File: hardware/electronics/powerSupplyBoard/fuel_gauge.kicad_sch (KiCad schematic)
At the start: 20 parts, among them J11 PREC002SAAN-RC, Q4 BSS84, Q5 2N7002, Q6 2N7002, U6 BQ34Z100-R2

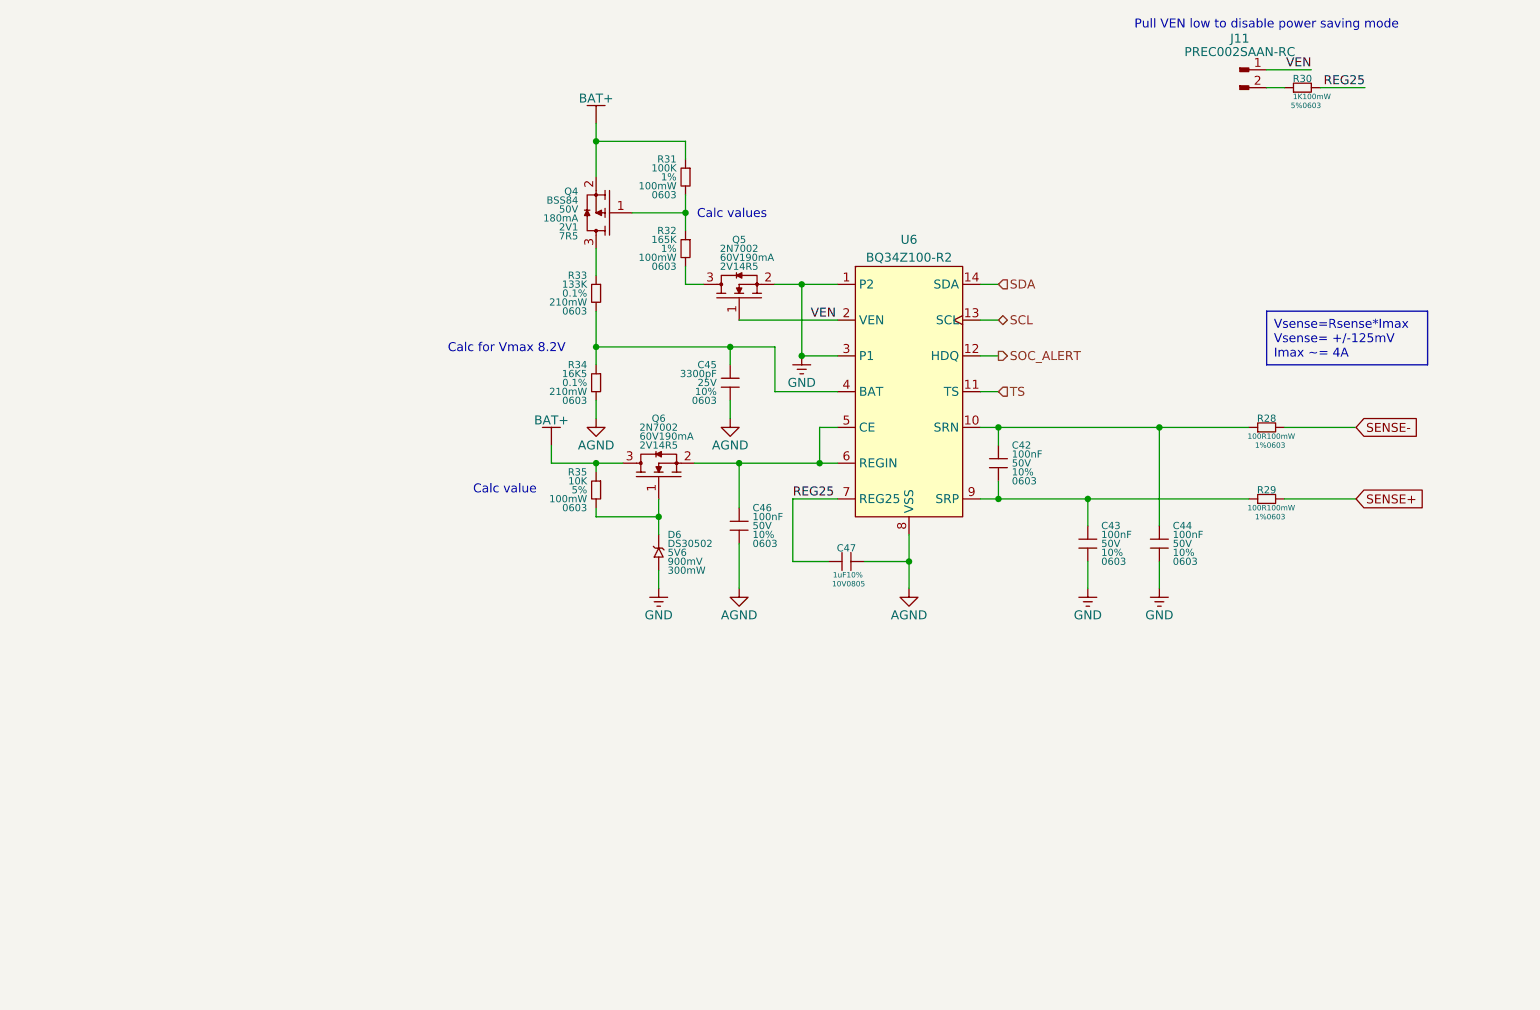
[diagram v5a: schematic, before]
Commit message: fixed component properties and added calculations for resistor dividers
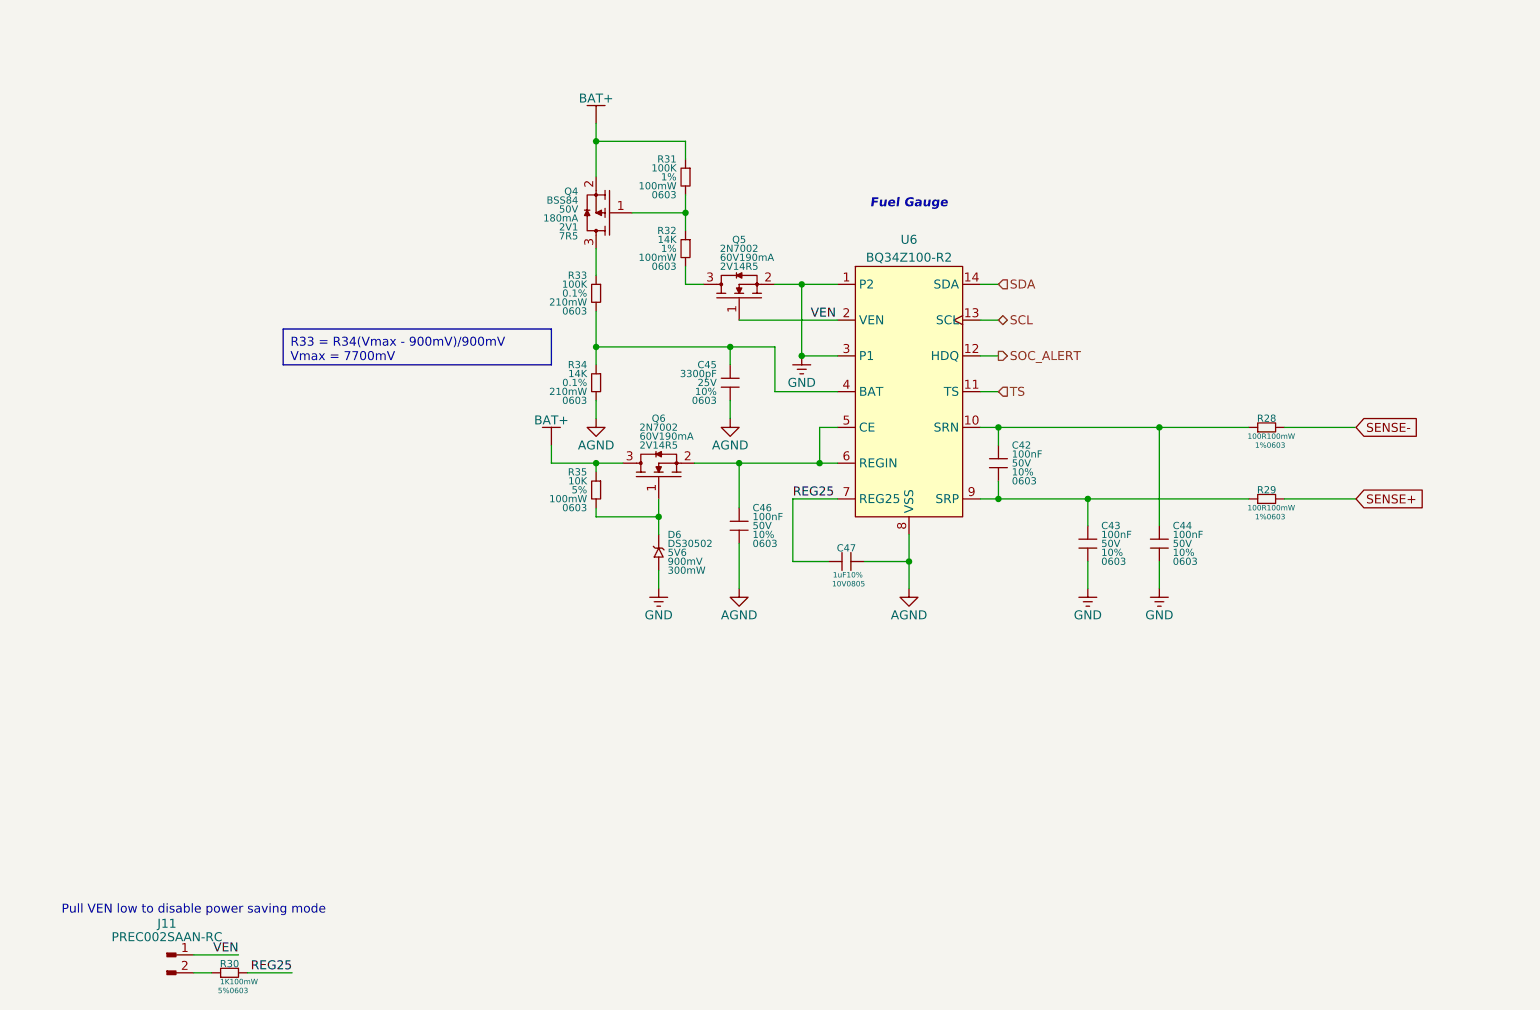
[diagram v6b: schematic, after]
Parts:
- R32: value 165K -> 14K; DKPN 541-165KHCT-ND -> 541-14.0KHCT-ND; MPN CRCW0603165KFKEA -> CRCW060314K0FKEA
- R33: value 133K -> 100K; DKPN 541-TNPW0603133KBEEACT-ND -> TNP100KAACT-ND; MPN TNPW0603133KBEEA -> TNPW0603100KBEEA
- R34: value 16K5 -> 14K; DKPN 541-3172-1-ND -> TNP14.0KAACT-ND; MPN TNPW060316K5BEEA -> TNPW060314K0BEEA
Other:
- note added: "Fuel Gauge"
- note removed: "Calc for Vmax 8.2V"
- note removed: "Calc value"
- note removed: "Calc values"
- moved on the sheet: J11, R30
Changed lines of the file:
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@@
 	(title_block
 		(title "LiFePO4 State of Charge")
-		(date "2024-11-01")
+		(date "2024-11-03")
 		(rev "01")
 		(comment 2 "PROTOTYPE")
@@
 	(wire
 		(pts
-			(xy 198.12 64.77) (xy 204.47 64.77)
+			(xy 45.72 190.5) (xy 52.07 190.5)
 		)
 		(stroke
@@
 	(wire
 		(pts
-			(xy 190.5 62.23) (xy 196.85 62.23)
+			(xy 38.1 187.96) (xy 44.45 187.96)
 		)
 		(stroke
@@
 	(wire
 		(pts
-			(xy 190.5 64.77) (xy 193.04 64.77)
+			(xy 38.1 190.5) (xy 40.64 190.5)
 		)
 		(stroke
@@
 		)
 	)
-	(text_box "Vsense=Rsense*Imax\nVsense= +/-125mV\nImax ~= 4A"
+	(text_box "R33 = R34(Vmax - 900mV)/900mV\nVmax = 7700mV"
 		(exclude_from_sim no)
-		(at 190.5 96.52 0)
-		(size 22.86 7.62)
+		(at 50.8 99.06 0)
+		(size 38.1 5.08)
 		(stroke
 			(width 0)
@@
 		)
 	)
-	(text "Calc for Vmax 8.2V"
+	(text "Fuel Gauge"
 		(exclude_from_sim no)
-		(at 82.55 101.854 0)
-		(effects
-			(font
-				(size 1.27 1.27)
-			)
-		)
-	)
-	(text "Calc values"
-		(exclude_from_sim no)
-		(at 114.554 82.804 0)
-		(effects
-			(font
-				(size 1.27 1.27)
-			)
-		)
-	)
-	(text "Calc value"
-		(exclude_from_sim no)
-		(at 82.296 121.92 0)
+		(at 139.7 81.28 0)
 		(effects
 			(font
 				(size 1.27 1.27)
+				(thickness 0.254)
+				(bold yes)
+				(italic yes)
 			)
 		)
@@
 	(text "Pull VEN low to disable power saving mode"
 		(exclude_from_sim no)
-		(at 190.5 55.88 0)
+		(at 38.1 181.61 0)
 		(effects
 			(font
@@
 	)
 	(label "REG25"
-		(at 204.47 64.77 180)
+		(at 52.07 190.5 180)
 		(fields_autoplaced yes)
 		(effects
@@
 	)
 	(label "VEN"
-		(at 196.85 62.23 180)
+		(at 44.45 187.96 180)
 		(fields_autoplaced yes)
 		(effects
@@
 			)
 		)
-		(property "Description" "Ceramic capacitor symbol"
+		(property "Description" "CAP CER 0.1UF 50V X7R 0603"
 			(at 165.1 129.54 0)
 			(effects
@@
 	(symbol
 		(lib_id "lib_sch:R_horizontal")
-		(at 195.58 64.77 0)
+		(at 43.18 190.5 0)
 		(unit 1)
 		(exclude_from_sim no)
@@
 		(fields_autoplaced yes)
 		(property "Reference" "R30"
-			(at 195.58 63.5 0)
+			(at 43.18 189.23 0)
 			(do_not_autoplace yes)
 			(effects
@@
 		)
 		(property "Value" "1K"
-			(at 195.58 66.04 0)
+			(at 43.18 191.77 0)
 			(do_not_autoplace yes)
 			(effects
@@
 		)
 		(property "Footprint" "DS-Resistors-SMD:CRCW0603"
-			(at 193.04 64.77 90)
+			(at 40.64 190.5 90)
 			(effects
 				(font
@@
 		)
 		(property "Datasheet" "datasheets/Vishay-Dale-DRCWe3.pdf"
-			(at 193.04 64.77 90)
+			(at 40.64 190.5 90)
 			(effects
 				(font
@@
 		)
 		(property "Description" "RES SMD 1K OHM 5% 1/10W 0603"
-			(at 195.58 64.77 0)
+			(at 43.18 190.5 0)
 			(effects
 				(font
@@
 		)
 		(property "Manufacturer" "Vishay Dale"
-			(at 193.04 64.77 90)
+			(at 40.64 190.5 90)
 			(effects
 				(font
@@
 		)
 		(property "MPN" "CRCW06031K00JNEA"
-			(at 193.04 64.77 90)
+			(at 40.64 190.5 90)
 			(effects
 				(font
@@
 		)
 		(property "DKPN" "541-1.0KGCT-ND"
-			(at 195.58 64.77 0)
+			(at 43.18 190.5 0)
 			(effects
 				(font
@@
 		)
 		(property "Tolerance" "5%"
-			(at 195.58 67.31 0)
+			(at 43.18 193.04 0)
 			(do_not_autoplace yes)
 			(effects
@@
 		)
 		(property "Power Rating" "100mW"
-			(at 195.58 66.04 0)
+			(at 43.18 191.77 0)
 			(do_not_autoplace yes)
 			(effects
@@
 		)
 		(property "Package" "0603"
-			(at 195.58 67.31 0)
+			(at 43.18 193.04 0)
 			(do_not_autoplace yes)
 			(effects
@@
 			)
 		)
-		(property "Value" "16K5"
+		(property "Value" "14K"
 			(at 93.98 105.41 0)
 			(do_not_autoplace yes)
@@
 			)
 		)
-		(property "Description" "RES 16.5K OHM 0.1% 0.21W 0603"
+		(property "Description" "RES 14K OHM 0.1% 0.21W 0603"
 			(at 95.25 106.68 0)
 			(effects
@@
 			)
 		)
-		(property "MPN" "TNPW060316K5BEEA"
+		(property "MPN" "TNPW060314K0BEEA"
 			(at 95.25 104.14 0)
 			(effects
@@
 			)
 		)
-		(property "DKPN" "541-3172-1-ND"
+		(property "DKPN" "TNP14.0KAACT-ND"
 			(at 95.25 106.68 0)
 			(effects
@@
 			)
 		)
-		(property "Description" "Ceramic capacitor symbol"
+		(property "Description" "CAP CER 0.1UF 50V X7R 0603"
 			(at 152.4 118.11 0)
 			(effects
@@
 			)
 		)
-		(property "Description" "Ceramic capacitor symbol"
+		(property "Description" "CAP CER 0.1UF 50V X7R 0603"
 			(at 115.57 127 0)
 			(effects
@@
 			)
 		)
-		(property "Description" "Ceramic capacitor symbol"
+		(property "Description" "CAP CER 0.1UF 50V X7R 0603"
 			(at 175.26 129.54 0)
 			(effects
@@
 			)
 		)
-		(property "Value" "133K"
+		(property "Value" "100K"
 			(at 93.98 92.71 0)
 			(do_not_autoplace yes)
@@
 			)
 		)
-		(property "Description" "RES 133K OHM 0.1% 0.21W 0603"
+		(property "Description" "RES 100K OHM 0.1% 0.21W 0603"
 			(at 95.25 93.98 0)
 			(effects
@@
 			)
 		)
-		(property "MPN" "TNPW0603133KBEEA"
+		(property "MPN" "TNPW0603100KBEEA"
 			(at 95.25 91.44 0)
 			(effects
@@
 			)
 		)
-		(property "DKPN" "541-TNPW0603133KBEEACT-ND"
+		(property "DKPN" "TNP100KAACT-ND"
 			(at 95.25 93.98 0)
 			(effects
@@
 	(symbol
 		(lib_id "lib_sch:Conn_01x02_Pin")
-		(at 186.69 63.5 0)
+		(at 34.29 189.23 0)
 		(unit 1)
 		(exclude_from_sim no)
@@
 		(fields_autoplaced yes)
 		(property "Reference" "J11"
-			(at 186.69 57.785 0)
+			(at 34.29 183.515 0)
 			(do_not_autoplace yes)
 			(effects
@@
 		)
 		(property "Value" "PREC002SAAN-RC"
-			(at 186.69 59.69 0)
+			(at 34.29 185.42 0)
 			(do_not_autoplace yes)
 			(effects
@@
 		)
 		(property "Footprint" "DS-Rectangular-Connectors:conn_01x02_254"
-			(at 187.96 64.77 0)
+			(at 35.56 190.5 0)
 			(effects
 				(font
@@
 		)
 		(property "Datasheet" "datasheets/Sullins-Connectors-zRzCzzzSzzN-RC.pdf"
-			(at 187.96 64.77 0)
+			(at 35.56 190.5 0)
 			(effects
 				(font
@@
 		)
 		(property "Description" "CONN HEADER VERT 2POS 2.54MM"
-			(at 187.96 64.77 0)
+			(at 35.56 190.5 0)
 			(effects
 				(font
@@
 		)
 		(property "Manufacturer" "Sullins Connector Solutions"
-			(at 187.96 64.77 0)
+			(at 35.56 190.5 0)
 			(effects
 				(font
@@
 		)
 		(property "MPN" "PREC002SAAN-RC"
-			(at 187.96 64.77 0)
+			(at 35.56 190.5 0)
 			(effects
 				(font
@@
 		)
 		(property "DKPN" "S1012EC-02-ND"
-			(at 187.96 64.77 0)
+			(at 35.56 190.5 0)
 			(effects
 				(font
@@
 			)
 		)
-		(property "Datasheet" "datasheets/Texas-Instruments-BQ34Z100-R2"
+		(property "Datasheet" "datasheets/Texas-Instruments-BQ34Z100-R2.pdf"
 			(at 139.7 107.95 0)
 			(effects
@@
 			)
 		)
-		(property "Value" "165K"
+		(property "Value" "14K"
 			(at 106.68 86.36 0)
 			(do_not_autoplace yes)
@@
 			)
 		)
-		(property "Description" "RES SMD 165K OHM 1% 1/10W 0603"
+		(property "Description" "RES SMD 14K OHM 1% 1/10W 0603"
 			(at 107.95 87.63 0)
 			(effects
@@
 			)
 		)
-		(property "MPN" "CRCW0603165KFKEA"
+		(property "MPN" "CRCW060314K0FKEA"
 			(at 107.95 85.09 0)
 			(effects
@@
 			)
 		)
-		(property "DKPN" "541-165KHCT-ND"
+		(property "DKPN" "541-14.0KHCT-ND"
 			(at 107.95 87.63 0)
 			(effects

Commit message: redefined footprint paths
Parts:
- C42, C43, C44, C46: footprint DS-Capacitors-SMD:MLCC0603 -> lib_fp:MLCC0603; MPN 06035C104K4T4A -> KAM15AR71H104KM
- C45: footprint DS-Capacitors-SMD:MLCC0603 -> lib_fp:MLCC0603
- C47: footprint DS-Capacitors-SMD:MLCC0805 -> lib_fp:MLCC0805
- D6: footprint DS-Package-SO:SOD523 -> lib_fp:SOD523
- J11: footprint DS-Rectangular-Connectors:conn_01x02_254 -> lib_fp:conn_01x02_254
- Q4, Q5, Q6: footprint DS-Package-SO:SOT23-3P95_290X130L43X40N -> lib_fp:SOT23-3P95_290X130L43X40N
- R28, R29, R30, R31, R32, R33, R34, R35: footprint DS-Resistors-SMD:CRCW0603 -> lib_fp:CRCW0603
- U6: footprint DS-Package-SO:TSSOP14P65_500x640X120L150X45N -> lib_fp:TSSOP14P65_500x640X120L150X45N
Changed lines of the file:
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@@
 			)
 		)
-		(property "Footprint" "DS-Package-SO:SOT23-3P95_290X130L43X40N"
+		(property "Footprint" "lib_fp:SOT23-3P95_290X130L43X40N"
 			(at 106.045 115.57 90)
 			(effects
@@
 			)
 		)
-		(property "Footprint" "DS-Capacitors-SMD:MLCC0603"
+		(property "Footprint" "lib_fp:MLCC0603"
 			(at 165.1 127.635 0)
 			(effects
@@
 			)
 		)
-		(property "MPN" "06035C104K4T4A"
+		(property "MPN" "KAM15AR71H104KM"
 			(at 165.1 127.635 0)
 			(effects
@@
 			)
 		)
-		(property "Footprint" "DS-Resistors-SMD:CRCW0603"
+		(property "Footprint" "lib_fp:CRCW0603"
 			(at 40.64 190.5 90)
 			(effects
@@
 			)
 		)
-		(property "Footprint" "DS-Resistors-SMD:CRCW0603"
+		(property "Footprint" "lib_fp:CRCW0603"
 			(at 107.95 74.93 0)
 			(effects
@@
 			)
 		)
-		(property "Footprint" "DS-Resistors-SMD:CRCW0603"
+		(property "Footprint" "lib_fp:CRCW0603"
 			(at 95.25 104.14 0)
 			(effects
@@
 			)
 		)
-		(property "Footprint" "DS-Capacitors-SMD:MLCC0603"
+		(property "Footprint" "lib_fp:MLCC0603"
 			(at 152.4 116.205 0)
 			(effects
@@
 			)
 		)
-		(property "MPN" "06035C104K4T4A"
+		(property "MPN" "KAM15AR71H104KM"
 			(at 152.4 116.205 0)
 			(effects
@@
 			)
 		)
-		(property "Footprint" "DS-Capacitors-SMD:MLCC0603"
+		(property "Footprint" "lib_fp:MLCC0603"
 			(at 115.57 125.095 0)
 			(effects
@@
 			)
 		)
-		(property "MPN" "06035C104K4T4A"
+		(property "MPN" "KAM15AR71H104KM"
 			(at 115.57 125.095 0)
 			(effects
@@
 			)
 		)
-		(property "Footprint" "DS-Capacitors-SMD:MLCC0603"
+		(property "Footprint" "lib_fp:MLCC0603"
 			(at 175.26 127.635 0)
 			(effects
@@
 			)
 		)
-		(property "MPN" "06035C104K4T4A"
+		(property "MPN" "KAM15AR71H104KM"
 			(at 175.26 127.635 0)
 			(effects
@@
 			)
 		)
-		(property "Footprint" "DS-Resistors-SMD:CRCW0603"
+		(property "Footprint" "lib_fp:CRCW0603"
 			(at 187.96 113.03 90)
 			(effects
@@
 			)
 		)
-		(property "Footprint" "DS-Package-SO:SOD523"
+		(property "Footprint" "lib_fp:SOD523"
 			(at 104.14 130.81 90)
 			(effects
@@
 			)
 		)
-		(property "Footprint" "DS-Capacitors-SMD:MLCC0603"
+		(property "Footprint" "lib_fp:MLCC0603"
 			(at 114.3 104.775 0)
 			(effects
@@
 			)
 		)
-		(property "Footprint" "DS-Resistors-SMD:CRCW0603"
+		(property "Footprint" "lib_fp:CRCW0603"
 			(at 95.25 91.44 0)
 			(effects
@@
 			)
 		)
-		(property "Footprint" "DS-Rectangular-Connectors:conn_01x02_254"
+		(property "Footprint" "lib_fp:conn_01x02_254"
 			(at 35.56 190.5 0)
 			(effects
@@
 			)
 		)
-		(property "Footprint" "DS-Resistors-SMD:CRCW0603"
+		(property "Footprint" "lib_fp:CRCW0603"
 			(at 95.25 119.38 0)
 			(effects
@@
 			)
 		)
-		(property "Footprint" "DS-Package-SO:SOT23-3P95_290X130L43X40N"
+		(property "Footprint" "lib_fp:SOT23-3P95_290X130L43X40N"
 			(at 117.475 90.17 90)
 			(effects
@@
 			)
 		)
-		(property "Footprint" "DS-Resistors-SMD:CRCW0603"
+		(property "Footprint" "lib_fp:CRCW0603"
 			(at 187.96 123.19 90)
 			(effects
@@
 			)
 		)
-		(property "Footprint" "DS-Package-SO:SOT23-3P95_290X130L43X40N"
+		(property "Footprint" "lib_fp:SOT23-3P95_290X130L43X40N"
 			(at 95.25 82.55 0)
 			(effects
@@
 			)
 		)
-		(property "Footprint" "DS-Package-SO:TSSOP14P65_500x640X120L150X45N"
+		(property "Footprint" "lib_fp:TSSOP14P65_500x640X120L150X45N"
 			(at 139.7 107.95 0)
 			(effects
@@
 			)
 		)
-		(property "Footprint" "DS-Resistors-SMD:CRCW0603"
+		(property "Footprint" "lib_fp:CRCW0603"
 			(at 107.95 85.09 0)
 			(effects
@@
 			)
 		)
-		(property "Footprint" "DS-Capacitors-SMD:MLCC0805"
+		(property "Footprint" "lib_fp:MLCC0805"
 			(at 130.81 137.795 0)
 			(effects

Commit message: updated component references and sizes
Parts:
- removed C47: 1uF, lib_fp:MLCC0805, symbol lib_sch:C_horizontal
- removed R29: 100R, lib_fp:CRCW0603, symbol lib_sch:R_horizontal
- removed R31: 100K, lib_fp:CRCW0603, symbol lib_sch:R
- removed R35: 10K, lib_fp:CRCW0603, symbol lib_sch:R
- added C46: 1uF, lib_fp:MLCC0603, symbol lib_sch:C_horizontal
- added R27: 100R, lib_fp:CRCW0402, symbol lib_sch:R_horizontal
- added R29: 100K, lib_fp:CRCW0402, symbol lib_sch:R
- added R33: 10K, lib_fp:CRCW0402, symbol lib_sch:R
- C44: renamed from C45; footprint lib_fp:MLCC0603 -> lib_fp:MLCC0402; DKPN 478-KGM15AR71E332KTCT-ND -> 478-KAM05AR71H332KHCT-ND; MPN KGM15AR71E332KT -> 04025C332K4T2A; Package 0603 -> 0402; Voltage Rating 25V -> 50V
- R28: footprint lib_fp:CRCW0603 -> lib_fp:CRCW0402; DKPN 541-100HCT-ND -> 541-100LCT-ND; MPN CRCW0603100RFKEA -> CRCW0402100RFKED; Package 0603 -> 0402; Power Rating 100mW -> 62.5mW
- R30: renamed from R32; footprint lib_fp:CRCW0603 -> lib_fp:CRCW0402; DKPN 541-14.0KHCT-ND -> 541-14.0KLCT-ND; MPN CRCW060314K0FKEA -> CRCW040214K0FKED; Package 0603 -> 0402; Power Rating 100mW -> 62.5mW
- R31: renamed from R33; footprint lib_fp:CRCW0603 -> lib_fp:CRCW0402; DKPN TNP100KAACT-ND -> TNP100KDACT-ND; MPN TNPW0603100KBEEA -> TNPW0402100KBEED; Package 0603 -> 0402; Power Rating 210mW -> 130mW
- R32: renamed from R34; footprint lib_fp:CRCW0603 -> lib_fp:CRCW0402; DKPN TNP14.0KAACT-ND -> 541-2075-1-ND; MPN TNPW060314K0BEEA -> TNPW040214K0BEED; Package 0603 -> 0402; Power Rating 210mW -> 130mW
- R34: renamed from R30; footprint lib_fp:CRCW0603 -> lib_fp:CRCW0402; DKPN 541-1.0KGCT-ND -> 541-1.0KJCT-ND; MPN CRCW06031K00JNEA -> CRCW04021K00JNED; Package 0603 -> 0402; Power Rating 100mW -> 62.5mW
- renumbered C42 to C41, C43 to C42, C44 to C43, C46 to C45
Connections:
- net AGND: now also C46.2
- net BAT+: now also R29.1, R33.1
- net REG25: now also C46.1
- net SENSE+: now also R28.2
- net SENSE-: now also R27.2; no longer R28.2
- net at D6.2, Q6.1: now also R33.2
- net at C41.2, C42.1, U6.9 (SRP): now also R28.1
- net at Q4.1, R30.1: now also R29.2
- net at C41.1, C43.1, U6.10 (SRN): now also R27.1; no longer R28.1
